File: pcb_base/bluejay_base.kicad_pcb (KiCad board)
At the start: 2 copper layers, 148.7 x 142.3 mm, 8 parts

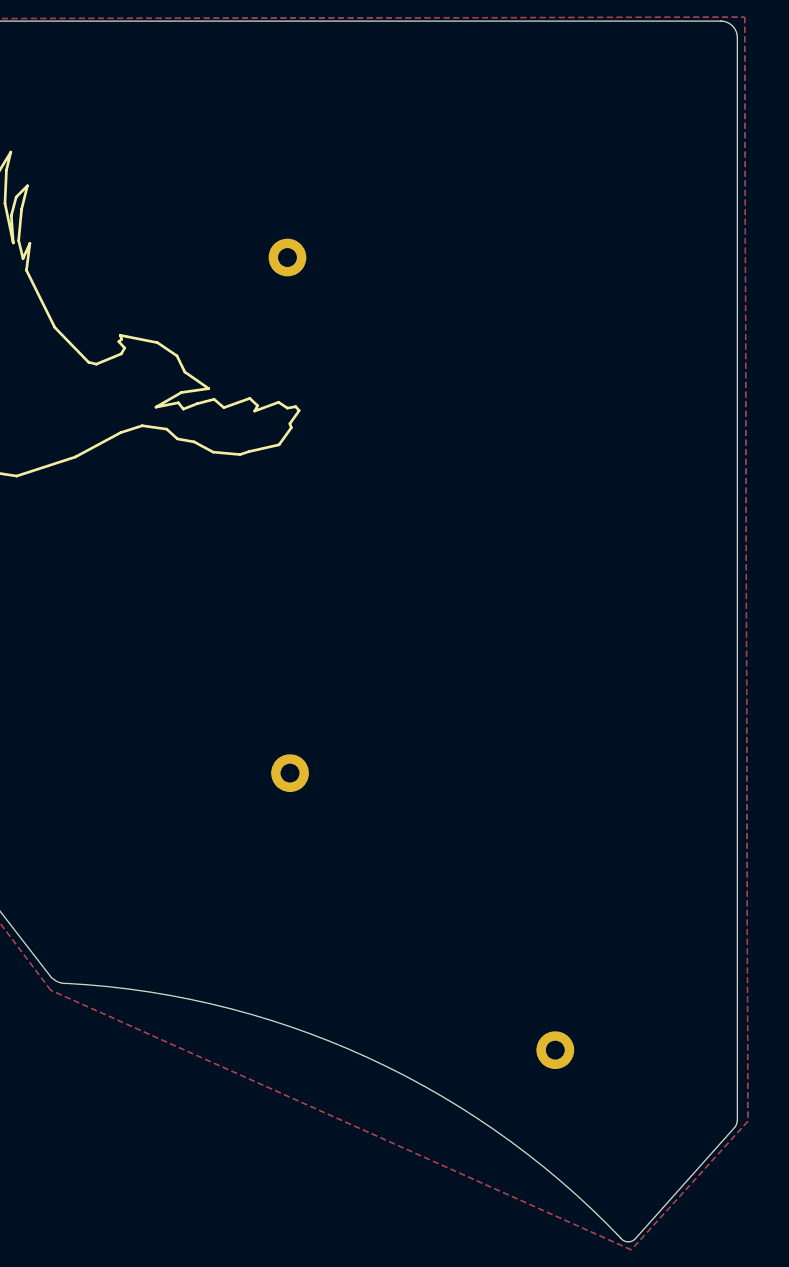
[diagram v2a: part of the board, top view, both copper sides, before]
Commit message: Fine tune edge cut
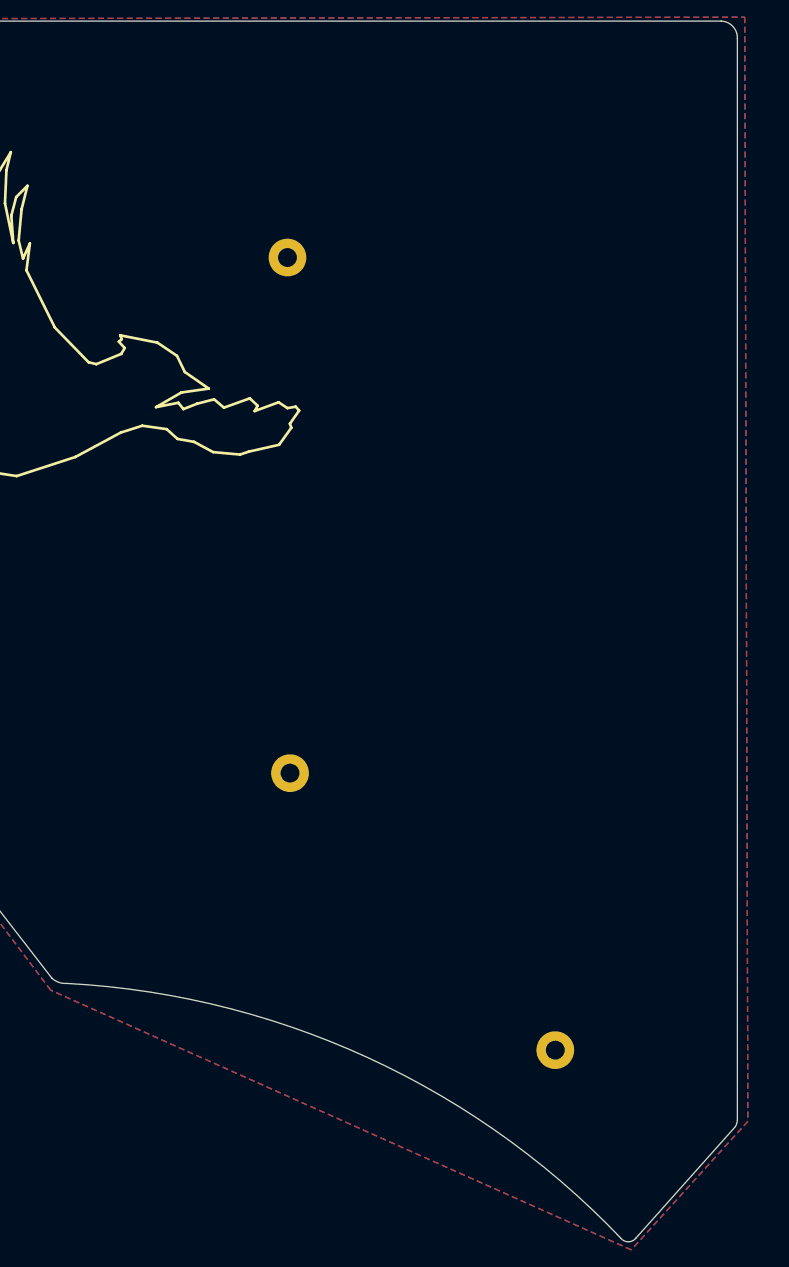
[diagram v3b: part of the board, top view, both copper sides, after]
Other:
- outline, holes or cut-outs redrawn
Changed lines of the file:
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@@
   (gr_arc (start -33.72 37.14) (mid -32.98386 37.23023) (end -32.31 37.54) (layer "Edge.Cuts") (width 0.1))
   (gr_arc (start -16.74 56.04) (mid 18.380681 64.696706) (end 47.83 85.7) (layer "Edge.Cuts") (width 0.1))
-  (gr_arc (start -16.74 56.04) (mid -17.619397 55.917949) (end -18.38 55.46) (layer "Edge.Cuts") (width 0.1))
-  (gr_arc (start 59.58 -56.175) (mid 60.933201 -55.55994) (end 61.46 -54.17) (layer "Edge.Cuts") (width 0.1))
+  (gr_arc (start -16.74 56.04) (mid -17.667469 55.912166) (end -18.47 55.43) (layer "Edge.Cuts") (width 0.1))
+  (gr_arc (start 59.58 -56.17) (mid 60.93217 -55.55744) (end 61.46 -54.17) (layer "Edge.Cuts") (width 0.1))
   (gr_line (start 61.46 72) (end 61.46 -54.17) (layer "Edge.Cuts") (width 0.1))
   (gr_arc (start -87.23 -54.18) (mid -86.647749 -55.594848) (end -85.23 -56.17) (layer "Edge.Cuts") (width 0.1))
@@
   (gr_arc (start 61.46 72) (mid 61.386012 72.382747) (end 61.23 72.74) (layer "Edge.Cuts") (width 0.1))
   (gr_line (start 59.58 -56.17) (end -85.23 -56.17) (layer "Edge.Cuts") (width 0.1))
-  (gr_arc (start 49.59 85.78) (mid 48.690274 86.173968) (end 47.83 85.7) (layer "Edge.Cuts") (width 0.1))
+  (gr_arc (start 49.62 85.75) (mid 48.712671 86.166365) (end 47.83 85.7) (layer "Edge.Cuts") (width 0.1))
   (gr_arc (start -33.72 36.84) (mid -32.960504 37.08023) (end -32.31 37.54) (layer "F.Fab") (width 0.1))
   (gr_arc (start 61.08 70.05) (mid 60.863331 70.823783) (end 60.48 71.53) (layer "F.Fab") (width 0.1))
